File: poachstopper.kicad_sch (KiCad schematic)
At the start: 6 parts, among them K2 G2RL-1A-E DC24, U1 NE555DR-MS

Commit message: draft created
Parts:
- removed K2: G2RL-1A-E DC24, easyeda2kicad:RELAY-TH_G2RL-1A-E, symbol easyeda2kicad:G2RL-1A-EDC24
- removed U1: NE555DR-MS, easyeda2kicad:SOIC-8_L4.9-W3.9-P1.27-LS6.0-BL, symbol easyeda2kicad:NE555DR-MS
- added J1, J2: XT60PW-M, kicad-import:CONN_XT60PW-M_AMA, symbol kicad-import:XT60PW-M
- added K1: G2RL-1A-E DC24, kicad-import:RELAY-TH_G2RL-1A-E, symbol kicad-import:G2RL-1A-EDC24
- added R3: 10, kicad-import:RES_3550_TEC-L, symbol kicad-import:355010RJT
- added U2: NE555DR-MS, kicad-import:SOIC-8_L4.9-W3.9-P1.27-LS6.0-BL, symbol kicad-import:NE555DR-MS
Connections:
- net 5V: now also U2.4 (RST), U2.8 (VCC)
- net GND: now also J1.2, J2.2, U2.1 (GND)
- net LATCH_CONTROL: now also K1.1
- net at C1.2, R1.1: now also U2.2 (TRIG), U2.6 (THRES)
- net at R2.2: now also U2.3 (OUT)
- new net: J2.1, K1.3, K1.4
- new net: K1.5, R3.2
- new net: J1.1, K1.6, R3.1
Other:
- moved on the sheet: C1, D1, R1, R2

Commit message: going running
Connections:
- net LATCH_CONTROL: now also D1.1 (K)
- net at K1.8: now also D1.2 (A)
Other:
- note added: "todo: 24v to 5v converter driver for the relay"
- moved on the sheet: D1
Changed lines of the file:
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@@
+		)
+	)
+	(text "todo: \n24v to 5v converter\ndriver for the relay"
+		(exclude_from_sim no)
+		(at 71.374 57.15 0)
+		(effects
+			(font
+				(size 1.27 1.27)
+			)
 		)
 	)
@@
 	)
 	(junction
+		(at 189.23 69.85)
+		(diameter 0)
+		(color 0 0 0 0)
+	)
+	(junction
+		(at 189.23 93.98)
+		(diameter 0)
+		(color 0 0 0 0)
+	)
+	(junction
 		(at 203.2 110.49)
 		(diameter 0)
@@
 	(wire
 		(pts
-			(xy 167.64 68.58) (xy 189.23 68.58)
+			(xy 166.37 64.77) (xy 189.23 64.77)
+		)
+		(stroke
+			(width 0)
+			(type default)
+		)
+	)
+	(wire
+		(pts
+			(xy 189.23 93.98) (xy 189.23 102.87)
 		)
 		(stroke
@@
 	(wire
 		(pts
+			(xy 189.23 69.85) (xy 189.23 64.77)
+		)
+		(stroke
+			(width 0)
+			(type default)
+		)
+	)
+	(wire
+		(pts
+			(xy 181.61 69.85) (xy 189.23 69.85)
+		)
+		(stroke
+			(width 0)
+			(type default)
+		)
+	)
+	(wire
+		(pts
 			(xy 129.54 83.82) (xy 129.54 91.44)
 		)
@@
 	(wire
 		(pts
+			(xy 189.23 90.17) (xy 189.23 93.98)
+		)
+		(stroke
+			(width 0)
+			(type default)
+		)
+	)
+	(wire
+		(pts
+			(xy 181.61 85.09) (xy 181.61 93.98)
+		)
+		(stroke
+			(width 0)
+			(type default)
+		)
+	)
+	(wire
+		(pts
 			(xy 104.14 91.44) (xy 99.06 91.44)
 		)
@@
 	(wire
 		(pts
+			(xy 181.61 93.98) (xy 189.23 93.98)
+		)
+		(stroke
+			(width 0)
+			(type default)
+		)
+	)
+	(wire
+		(pts
 			(xy 203.2 90.17) (xy 203.2 95.25)
 		)
@@
 	(wire
 		(pts
-			(xy 189.23 72.39) (xy 189.23 68.58)
+			(xy 189.23 72.39) (xy 189.23 69.85)
 		)
 		(stroke
@@
 	(wire
 		(pts
+			(xy 181.61 77.47) (xy 181.61 69.85)
+		)
+		(stroke
+			(width 0)
+			(type default)
+		)
+	)
+	(wire
+		(pts
 			(xy 203.2 63.5) (xy 203.2 68.58)
 		)
@@
 	)
 	(label "LATCH_CONTROL"
-		(at 167.64 68.58 0)
+		(at 166.37 64.77 0)
 		(effects
 			(font
@@
 	(symbol
 		(lib_id "PCM_Diode_AKL:1N4007")
-		(at 173.99 81.28 270)
+		(at 181.61 81.28 90)
 		(unit 1)
 		(body_style 1)
@@
 		(in_pos_files yes)
 		(dnp no)
-		(fields_autoplaced yes)
 		(property "Reference" "D1"
-			(at 176.53 80.0099 90)
+			(at 174.498 82.042 90)
 			(show_name no)
 			(do_not_autoplace no)
@@
 		)
 		(property "Value" "1N4007"
-			(at 176.53 82.5499 90)
+			(at 179.324 80.264 90)
 			(show_name no)
 			(do_not_autoplace no)
@@
 		)
 		(property "Footprint" "PCM_Diode_THT_AKL:D_DO-41_SOD81_P7.62mm_Horizontal"
-			(at 173.99 81.28 0)
+			(at 181.61 81.28 0)
 			(hide yes)
 			(show_name no)
@@
 		)
 		(property "Datasheet" "https://www.tme.eu/Document/5f8ffc5ac30fc86bac97d66040bf5502/1n400x.pdf"
-			(at 173.99 81.28 0)
+			(at 181.61 81.28 0)
 			(hide yes)
 			(show_name no)
@@
 		)
 		(property "Description" "DO-41 Diode, Rectifier, 1000V, 1A, Alternate KiCad Library"
-			(at 173.99 81.28 0)
-			(hide yes)
-			(show_name no)
+			(at 181.61 81.28 0)
+			(hide yes)
+			(show_name no)

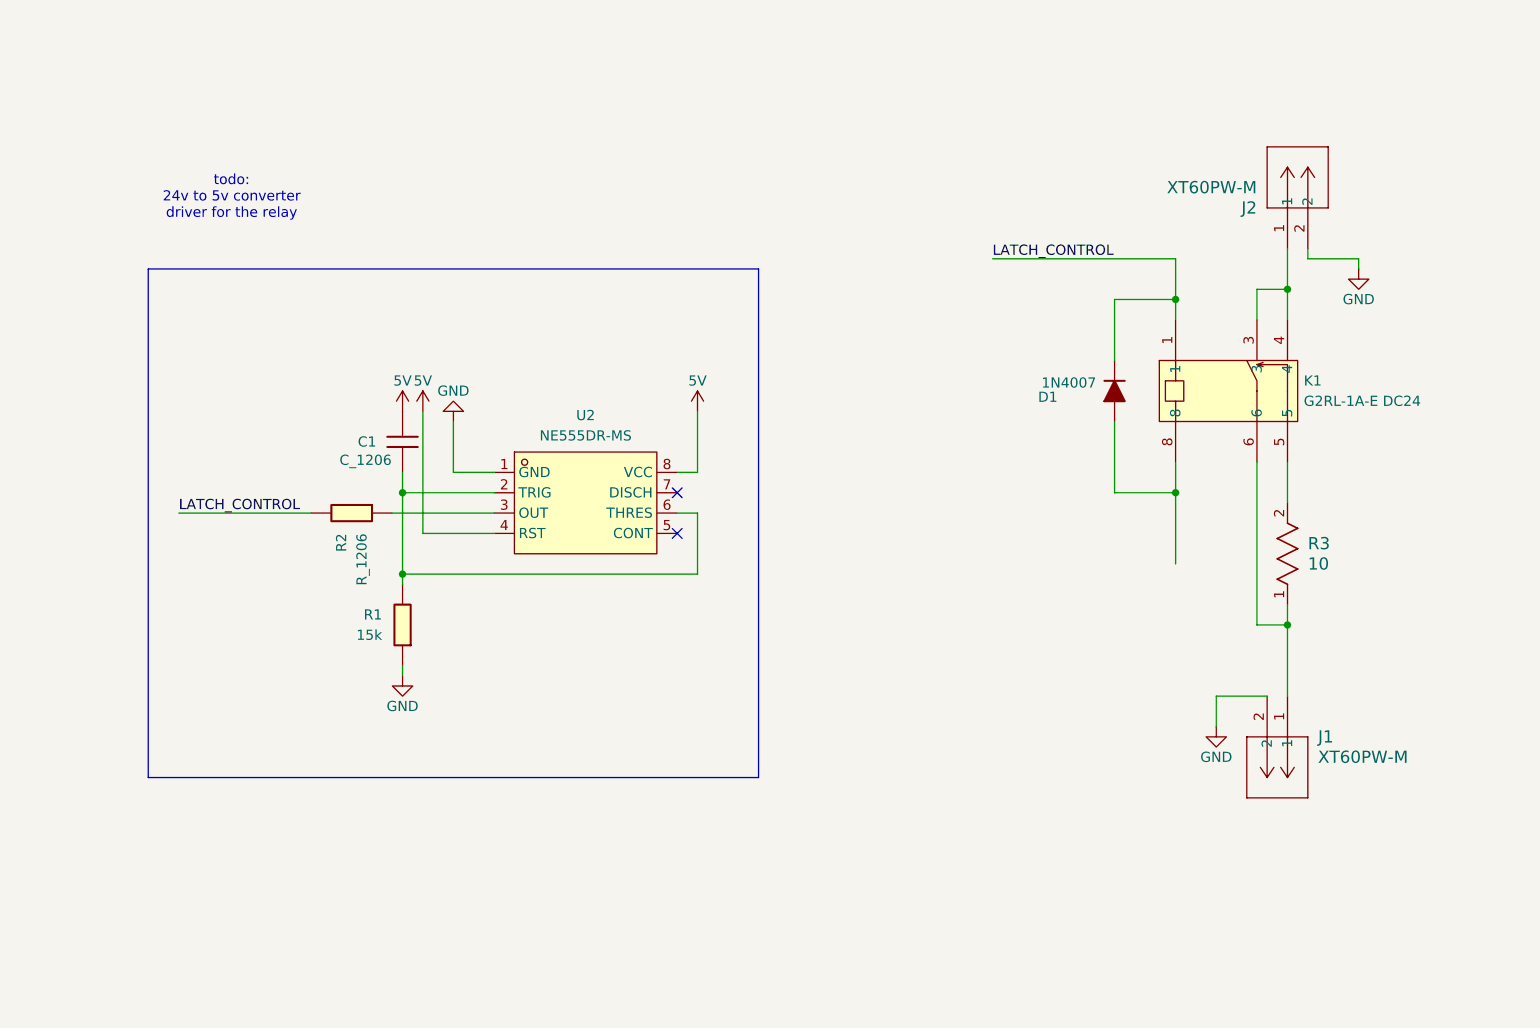
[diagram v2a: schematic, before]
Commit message: circuit cleanup, functionality finalized, BOM
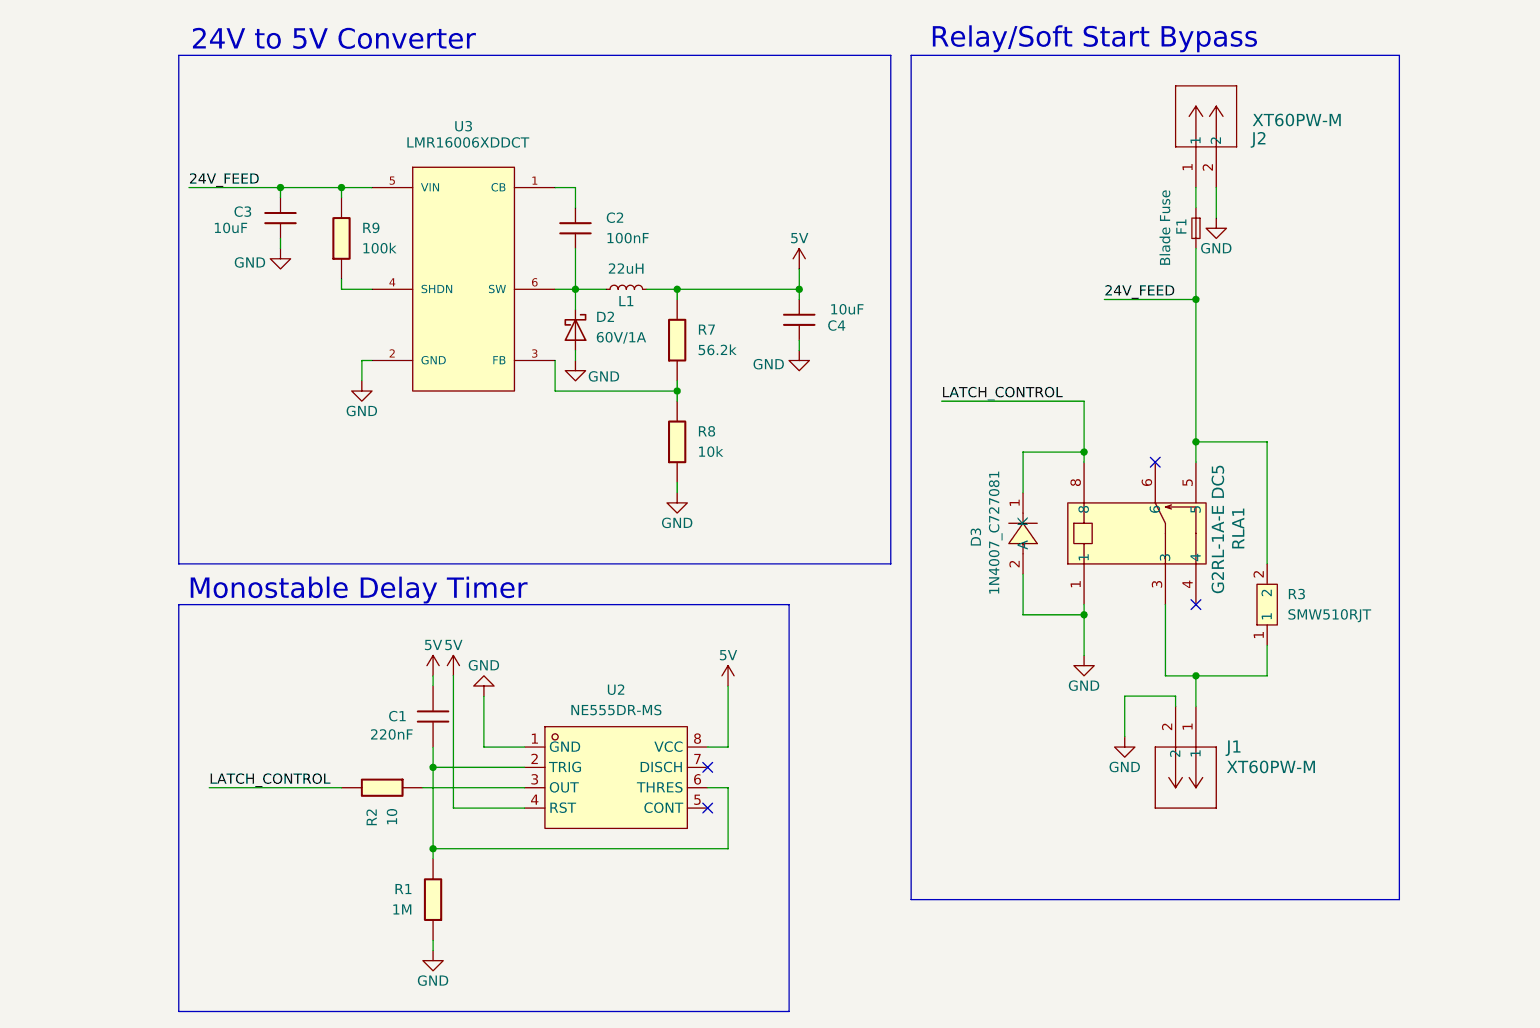
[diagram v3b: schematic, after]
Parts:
- removed D1: 1N4007, PCM_Diode_THT_AKL:D_DO-41_SOD81_P7.62mm_Horizontal, symbol PCM_Diode_AKL:1N4007
- removed K1: G2RL-1A-E DC24, kicad-import:RELAY-TH_G2RL-1A-E, symbol kicad-import:G2RL-1A-EDC24
- removed R3: 10, kicad-import:RES_3550_TEC-L, symbol kicad-import:355010RJT
- added C2: 100nF, PCM_fab:C_1206, symbol PCM_fab:C_1206
- added C3, C4: 10uF, PCM_fab:C_1206, symbol PCM_fab:C_1206
- added D2: 60V/1A, PCM_fab:Diode_Schottky_0603, symbol PCM_fab:Diode_Schottky_0603
- added D3: 1N4007_C727081, kicad-import:SMA_L4.3-W2.5-LS5.0-RD, symbol kicad-import:1N4007_C727081
- added F1: Blade Fuse, PCM_SparkFun-Fuse:Fuseholder_Automotive, symbol PCM_SparkFun-Fuse:Fuse_Holder-Blade
- added L1: 22uH, PCM_SparkFun-Coil:0805, symbol PCM_SparkFun-Coil:1.0uH_0805_1.45A
- added R3: SMW510RJT, kicad-import:RES-SMD_L13.5-W7.3, symbol kicad-import:SMW510RJT
- added R7: 56.2k, PCM_fab:R_1206, symbol PCM_fab:R_1206
- added R8: 10k, PCM_fab:R_1206, symbol PCM_fab:R_1206
- added R9: 100k, PCM_fab:R_1206, symbol PCM_fab:R_1206
- added RLA1: G2RL-1A-E DC5, kicad-import:RELAY_G2RL-1A-E_DC5_OMR, symbol kicad-import:G2RL-1A-E_DC5
- added U3: LMR16006XDDCT, kicad-import:SOT95P280X110-6N, symbol kicad-import:LMR16006XDDCT
- C1: value C_1206 -> 220nF
- R1: value 15k -> 1M
- R2: value R_1206 -> 10
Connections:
- net 5V: now also C4.2, L1.2, R7.1
- net GND: now also C3.2, C4.1, D2.2 (A), D3.2 (A), R8.2, RLA1.1, U3.2 (GND)
- net LATCH_CONTROL: now also D3.1 (K), RLA1.8
- net at J2.1: now also F1.1
- net at J1.1: now also R3.1, RLA1.3
- new net: R7.2, R8.1, U3.3 (FB)
- new net: C2.1, U3.1 (CB)
- new net: C2.2, D2.1 (K), L1.1, U3.6 (SW)
- new net: R9.2, U3.4 (SHDN)
- new net 24V_FEED: C3.1, F1.2, R3.2, R9.1, RLA1.5, U3.5 (VIN)
- no-connect marks 2 -> 4
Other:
- note added: "24V to 5V Converter"
- note added: "Monostable Delay Timer"
- note added: "Relay/Soft Start Bypass"
- note removed: "todo: 24v to 5v converter driver for the relay"
- moved on the sheet: C1, J1, J2, R1, R2, U2
